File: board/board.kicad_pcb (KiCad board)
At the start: 4 copper layers, 53 x 39.5 mm, 38 parts, among them J1 ANT, J2 DEBUG, J3 GPIO, J4 USB_B_Micro, SW1 BOOTSEL, SW2 RUN, U1 RP2040, U2 W25Q128JVS, U3 NCP1117-3.3_SOT223, U4 RFM95W-915S2, U5 BLE5201, Y1 ABM8G-12.000MHZ-18-D2Y-T

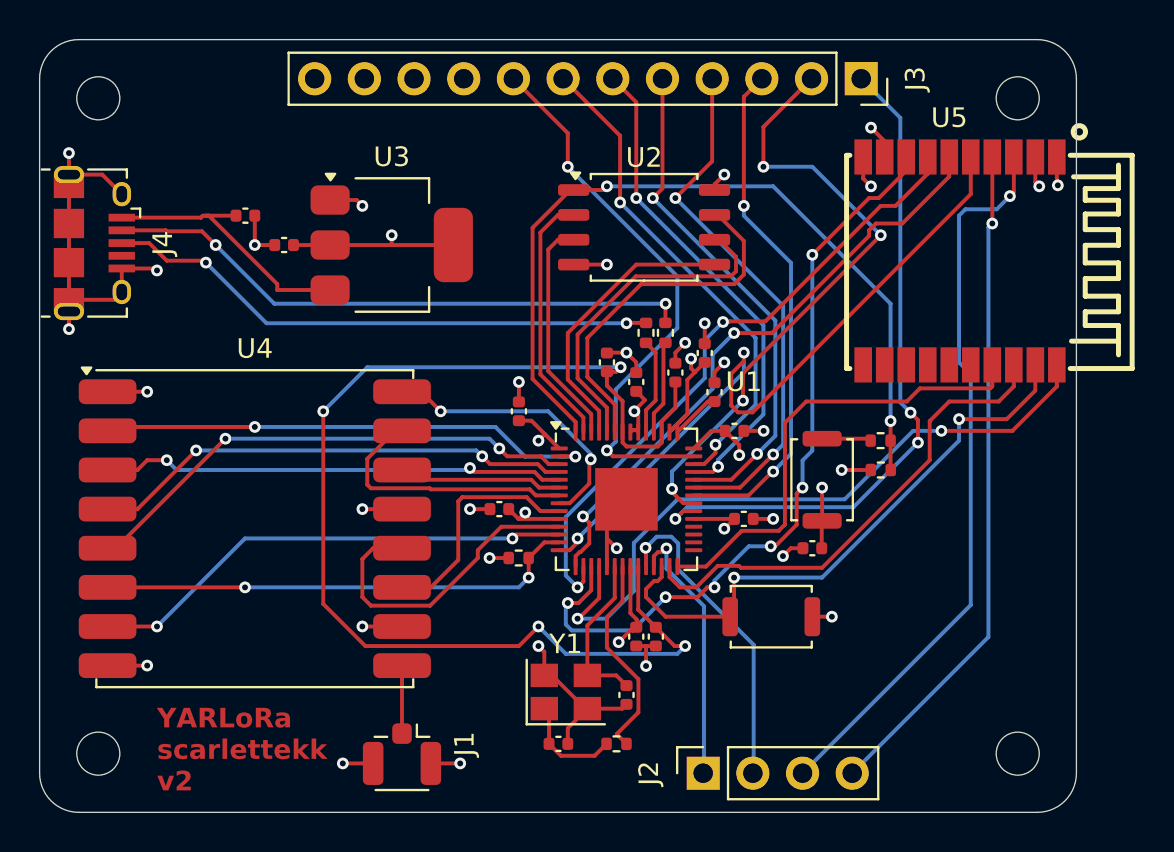
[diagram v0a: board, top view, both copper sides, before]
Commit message: appease jlcpcb (component swaps)
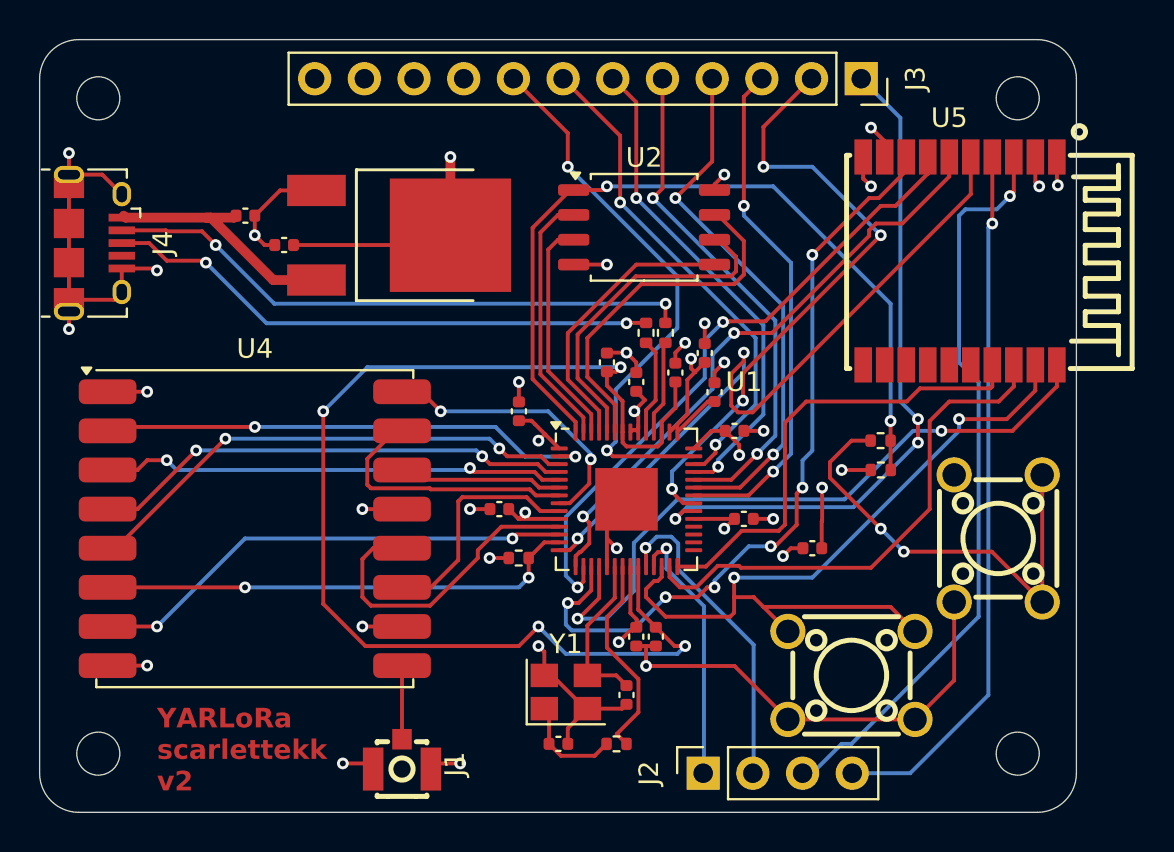
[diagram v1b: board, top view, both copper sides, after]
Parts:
- J1: footprint Connector_Coaxial:U.FL_Hirose_U.FL-R-SMT-1_Vertical -> BWU.FL-IPEX1:BWU.FL-IPEX1
- SW1, SW2: footprint Button_Switch_SMD:SW_Push_SPST_NO_Alps_SKRK -> K2-1102DP-L3SW-04:SW-TH_4P-L6.0-W6.0-P4.50-LS6.5
- U3: value NCP1117-3.3_SOT223 -> NCP1117DT33G; footprint Package_TO_SOT_SMD:SOT-223-3_TabPin2 -> NCP1117DT50G:NCP1117DT50G
- moved SW1 9.49 mm to (91.0, 52.0)
- moved SW2 5.08 mm to (83.5, 59.0)
- moved U3 0.66 mm to (59.6, 36.5), turned to 180 degrees
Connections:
- SW1 pad 2: Net-(R6-Pad1) -> GND
- SW2 pad 2: /RUN -> GND
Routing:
- net GND: track 64.5 -> 88.4 mm, vias 26 -> 24
- net Net-(R6-Pad1): track 2.52 -> 23.5 mm, vias 0 -> 2
- net /RUN: track 30.1 -> 41.6 mm
- net +3V3: track 46.7 -> 50.3 mm
- net /BLE_SWDIO: track 34.5 -> 36.2 mm
- net /PB01: track 25.0 -> 26.4 mm
- net VBUS: track 14.0 -> 12.8 mm
- net /BLE_SWCLK: track 37.4 -> 38.3 mm
